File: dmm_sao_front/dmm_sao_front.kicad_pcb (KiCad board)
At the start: 2 copper layers, 37 x 71 mm, 7 parts

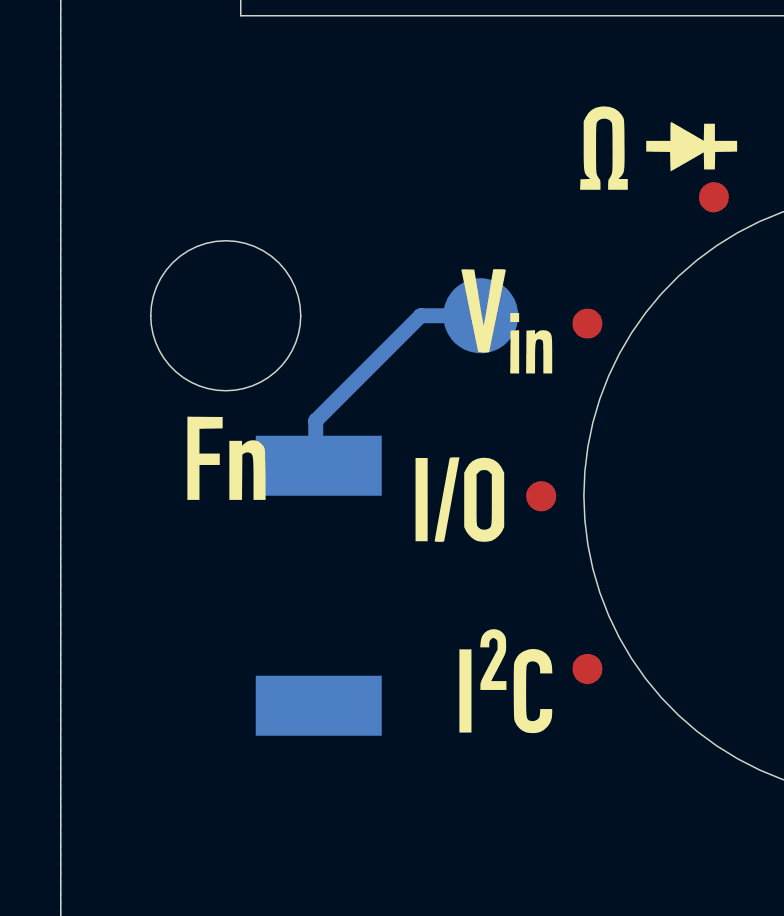
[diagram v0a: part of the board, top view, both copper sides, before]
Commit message: Moved buzzer to base board
Also:
- Moved a few parts to make space for the buzzer
- Connected the buzzer in a push/pull setup for better volume
- Changed the edgecut a little, to have better space for knob intent mechanism in case
- Tweaked pads for spring loaded pins to match manufacturer suggestion
- Made the paste for the display connector 10% smaller

Signed-off-by: Thomas Flummer <tf@flummer.net>
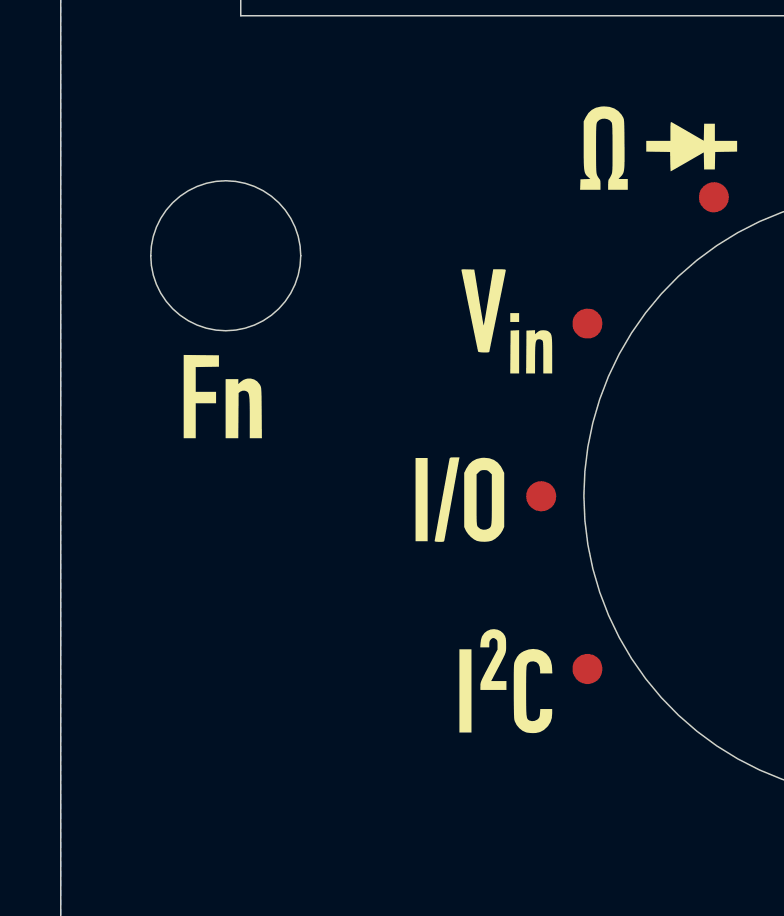
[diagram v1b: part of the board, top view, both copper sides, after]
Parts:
- removed the REF** at (95.5, 96.0)
- removed the REF** at (90.1, 105.0)
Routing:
- net BUZZER: track 8.45 -> 0.00 mm
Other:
- outline, holes or cut-outs redrawn
- board text removed: "BUZZER"
